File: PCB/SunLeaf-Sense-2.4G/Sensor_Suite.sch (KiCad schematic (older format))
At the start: 0 parts

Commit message: Sensors Added
Sensors added to schematic page, project setup around new 2G module from ST
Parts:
- added M?: SCD30, AVR-KiCAD-Lib-Modules:MODULE_SCD30, symbol AVR-KiCAD-Lib-Modules:SCD30
- added U?: AS7341-DLGT, AVR-KiCAD-Lib-ICs:AS7341-DLGT, symbol AVR-KiCAD-Lib-ICs:AS7341-DLGT
- added U? (x2): HDC1080DMBR, AVR-KiCAD-Lib-ICs:HDC1080DMBR, symbol AVR-KiCAD-Lib-ICs:HDC1080DMBR
- added U?: TPIS1T1086_L5.5, AVR-KiCAD-Lib-ICs:TPIS 1T 1086 L5.5, symbol AVR-KiCAD-Lib-ICs:TPIS1T1086_L5.5
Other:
- note added: "CO2 Sensor Module"
- note added: "Light Spectrum Sensor"
- note added: "Optical IR Sensor"
- note added: "Temperature and Humidity Sensors"
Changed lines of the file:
@@
 $Descr A4 11693 8268
 encoding utf-8
-Sheet 1 5
+Sheet 3 4
 Title ""
 Date ""
@@
 Comment4 ""
 $EndDescr
+$Comp
+L AVR-KiCAD-Lib-Modules:SCD30 M?
+U 1 1 603BC534
+P 3100 3200
+F 0 "M?" H 3150 3250 50  0000 C CNN
+F 1 "SCD30" H 3150 3400 50  0001 C CNN
+F 2 "AVR-KiCAD-Lib-Modules:MODULE_SCD30" H 2900 3200 50  0001 C CNN
+F 3 "https://media.digikey.com/pdf/Data%20Sheets/Sensirion%20PDFs/CD_DS_SCD30_Datasheet_D1.pdf" H 3000 3300 50  0001 C CNN
+F 4 "54.00000" H 3200 3450 50  0001 C CNN "Cost QTY: 1"
+F 5 "*" H 3300 3550 50  0001 C CNN "Cost QTY: 1000"
+F 6 "*" H 3400 3650 50  0001 C CNN "Cost QTY: 2500"
+F 7 "*" H 3500 3750 50  0001 C CNN "Cost QTY: 5000"
+F 8 "*" H 3600 3850 50  0001 C CNN "Cost QTY: 10000"
+F 9 "Sensirion AG" H 3700 3950 50  0001 C CNN "MFR"
+F 10 "SCD30" H 3800 4050 50  0001 C CNN "MFR#"
+F 11 "Digikey" H 3900 4150 50  0001 C CNN "Vendor"
+F 12 "1649-1098-ND" H 4000 4250 50  0001 C CNN "Vendor #"
+F 13 "AVR" H 4100 4350 50  0001 C CNN "Designer"
+F 14 "*" H 4200 4450 50  0001 C CNN "Height"
+F 15 "2/25/2021" H 5300 5550 50  0001 C CNN "Date Created"
+F 16 "2/25/2021" H 4300 4550 50  0001 C CNN "Date Modified"
+F 17 "Yes" H 4400 4650 50  0001 C CNN "Lead-Free ?"
+F 18 "1" H 4500 4750 50  0001 C CNN "RoHS Levels"
+F 19 "ThroughHole" H 4600 4850 50  0001 C CNN "Mounting"
+F 20 "7" H 4700 4950 50  0001 C CNN "Pin Count #"
+F 21 "Active" H 4800 5050 50  0001 C CNN "Status"
+F 22 "*" H 4900 5150 50  0001 C CNN "Tolerance"
+F 23 "CO2 Sensor" H 5000 5250 50  0001 C CNN "Type"
+F 24 "3.3V-5.5V" H 5100 5350 50  0001 C CNN "Voltage"
+F 25 "*" H 5200 5500 50  0001 C CNN "Package"
+F 26 "Carbon Dioxide (CO2) Sensor I²C, Modbus, PWM" H 5500 5800 50  0001 C CNN "Description"
+F 27 "SCD30" H 3200 2350 50  0000 C CNN "_Value_"
+F 28 "*" H 5500 5800 50  0001 C CNN "Management_ID"
+	1    3100 3200
+	1    0    0    -1
+$EndComp
+$Comp
+L AVR-KiCAD-Lib-ICs:AS7341-DLGT U?
+U 1 1 603BEEB8
+P 8900 3050
+F 0 "U?" H 8950 3100 50  0000 C CNN
+F 1 "AS7341-DLGT" H 9000 3250 50  0001 C CNN
+F 2 "AVR-KiCAD-Lib-ICs:AS7341-DLGT" H 8800 2850 50  0001 C CNN
+F 3 "https://media.digikey.com/pdf/Data%20Sheets/Austriamicrosystems%20PDFs/AS7341_DS.pdf" H 8900 2950 50  0001 C CNN
+F 4 "6.75000" H 9000 3300 50  0001 C CNN "Cost QTY: 1"
+F 5 "4.20000" H 9100 3400 50  0001 C CNN "Cost QTY: 1000"
+F 6 "*" H 9200 3500 50  0001 C CNN "Cost QTY: 2500"
+F 7 "*" H 9300 3600 50  0001 C CNN "Cost QTY: 5000"
+F 8 "*" H 9400 3700 50  0001 C CNN "Cost QTY: 10000"
+F 9 "AMS" H 9500 3800 50  0001 C CNN "MFR"
+F 10 "AS7341-DLGT" H 9600 3900 50  0001 C CNN "MFR#"
+F 11 "Digikey" H 9700 4000 50  0001 C CNN "Vendor"
+F 12 "AS7341-DLGTTR-ND" H 9800 4100 50  0001 C CNN "Vendor #"
+F 13 "AVR" H 9900 4200 50  0001 C CNN "Designer"
+F 14 "1mm" H 10000 4300 50  0001 C CNN "Height"
+F 15 "2/25/2021" H 11100 5400 50  0001 C CNN "Date Created"
+F 16 "2/25/2021" H 10100 4400 50  0001 C CNN "Date Modified"
+F 17 "Yes" H 10200 4500 50  0001 C CNN "Lead-Free ?"
+F 18 "1" H 10300 4600 50  0001 C CNN "RoHS Levels"
+F 19 "SMT" H 10400 4700 50  0001 C CNN "Mounting"
+F 20 "8" H 10500 4800 50  0001 C CNN "Pin Count #"
+F 21 "Active" H 10600 4900 50  0001 C CNN "Status"
+F 22 "*" H 10700 5000 50  0001 C CNN "Tolerance"
+F 23 "Light Sensor" H 10800 5100 50  0001 C CNN "Type"
+F 24 "1.8V" H 10900 5200 50  0001 C CNN "Voltage"
+F 25 "8-TFLGA" H 11000 5350 50  0001 C CNN "Package"
+F 26 "Optical Sensor Ambient  I²C 8-TFLGA" H 11300 5650 50  0001 C CNN "Description"
+F 27 "AS7341-DLGT" H 9150 2500 50  0000 C CNN "_Value_"
+F 28 "*" H 11300 5650 50  0001 C CNN "Management_ID"
+	1    8900 3050
+	1    0    0    -1
+$EndComp
+$Comp
+L AVR-KiCAD-Lib-ICs:HDC1080DMBR U?
+U 1 1 603C9047
+P 9450 4350
+F 0 "U?" H 10000 4400 50  0000 C CNN
+F 1 "HDC1080DMBR" H 9500 4450 50  0001 C CNN
+F 2 "AVR-KiCAD-Lib-ICs:HDC1080DMBR" H 9550 4950 50  0001 C CNN
+F 3 "https://www.ti.com/lit/ds/symlink/hdc1080.pdf?HQS=dis-dk-null-digikeymode-dsf-pf-null-wwe&ts=1614238925919" H 9350 4350 50  0001 C CNN
+F 4 "2.80000" H 9550 4600 50  0001 C CNN "Cost QTY: 1"
+F 5 "1.53120" H 9650 4700 50  0001 C CNN "Cost QTY: 1000"
+F 6 "*" H 9750 4800 50  0001 C CNN "Cost QTY: 2500"
+F 7 "*" H 9850 4900 50  0001 C CNN "Cost QTY: 5000"
+F 8 "*" H 9950 5000 50  0001 C CNN "Cost QTY: 10000"
+F 9 "Texas Instruments" H 10050 5100 50  0001 C CNN "MFR"
+F 10 "HDC1080DMBR" H 10150 5200 50  0001 C CNN "MFR#"
+F 11 "Digikey" H 10250 5300 50  0001 C CNN "Vendor"
+F 12 "296-46272-2-ND" H 10350 5400 50  0001 C CNN "Vendor #"
+F 13 "AVR" H 10450 5500 50  0001 C CNN "Designer"
+F 14 "0.8mm" H 10550 5600 50  0001 C CNN "Height"
+F 15 "2/25/2021" H 11650 6700 50  0001 C CNN "Date Created"
+F 16 "2/25/2021" H 10650 5700 50  0001 C CNN "Date Modified"
+F 17 "Yes" H 10750 5800 50  0001 C CNN "Lead-Free ?"
+F 18 "1" H 10850 5900 50  0001 C CNN "RoHS Levels"
+F 19 "SMT" H 10950 6000 50  0001 C CNN "Mounting"
+F 20 "6" H 11050 6100 50  0001 C CNN "Pin Count #"
+F 21 "Active" H 11150 6200 50  0001 C CNN "Status"
+F 22 "*" H 11250 6300 50  0001 C CNN "Tolerance"
+F 23 "Temp/Humid Sensor" H 11350 6400 50  0001 C CNN "Type"
+F 24 "2.7-5.5V" H 11450 6500 50  0001 C CNN "Voltage"
+F 25 "6-WASON" H 11550 6650 50  0001 C CNN "Package"
+F 26 "Humidity Temperature Sensor 0 ~ 100% RH I²C ±2% RH 15s Surface Mount" H 11850 6950 50  0001 C CNN "Description"
+F 27 "HDC1080DMBR" H 9750 3700 50  0000 C CNN "_Value_"
+F 28 "*" H 11850 6950 50  0001 C CNN "Management_ID"
+	1    9450 4350
+	-1   0    0    -1
+$EndComp
+$Comp
+L AVR-KiCAD-Lib-ICs:HDC1080DMBR U?
+U 1 1 603CFAB5
+P 9450 5400
+F 0 "U?" H 10000 5450 50  0000 C CNN
+F 1 "HDC1080DMBR" H 9500 5500 50  0001 C CNN
+F 2 "AVR-KiCAD-Lib-ICs:HDC1080DMBR" H 9550 6000 50  0001 C CNN
+F 3 "https://www.ti.com/lit/ds/symlink/hdc1080.pdf?HQS=dis-dk-null-digikeymode-dsf-pf-null-wwe&ts=1614238925919" H 9350 5400 50  0001 C CNN
+F 4 "2.80000" H 9550 5650 50  0001 C CNN "Cost QTY: 1"
+F 5 "1.53120" H 9650 5750 50  0001 C CNN "Cost QTY: 1000"
+F 6 "*" H 9750 5850 50  0001 C CNN "Cost QTY: 2500"
+F 7 "*" H 9850 5950 50  0001 C CNN "Cost QTY: 5000"
+F 8 "*" H 9950 6050 50  0001 C CNN "Cost QTY: 10000"
+F 9 "Texas Instruments" H 10050 6150 50  0001 C CNN "MFR"
+F 10 "HDC1080DMBR" H 10150 6250 50  0001 C CNN "MFR#"
+F 11 "Digikey" H 10250 6350 50  0001 C CNN "Vendor"
+F 12 "296-46272-2-ND" H 10350 6450 50  0001 C CNN "Vendor #"
+F 13 "AVR" H 10450 6550 50  0001 C CNN "Designer"
+F 14 "0.8mm" H 10550 6650 50  0001 C CNN "Height"
+F 15 "2/25/2021" H 11650 7750 50  0001 C CNN "Date Created"
+F 16 "2/25/2021" H 10650 6750 50  0001 C CNN "Date Modified"
+F 17 "Yes" H 10750 6850 50  0001 C CNN "Lead-Free ?"
+F 18 "1" H 10850 6950 50  0001 C CNN "RoHS Levels"
+F 19 "SMT" H 10950 7050 50  0001 C CNN "Mounting"
+F 20 "6" H 11050 7150 50  0001 C CNN "Pin Count #"
+F 21 "Active" H 11150 7250 50  0001 C CNN "Status"
+F 22 "*" H 11250 7350 50  0001 C CNN "Tolerance"
+F 23 "Temp/Humid Sensor" H 11350 7450 50  0001 C CNN "Type"
+F 24 "2.7-5.5V" H 11450 7550 50  0001 C CNN "Voltage"
+F 25 "6-WASON" H 11550 7700 50  0001 C CNN "Package"
+F 26 "Humidity Temperature Sensor 0 ~ 100% RH I²C ±2% RH 15s Surface Mount" H 11850 8000 50  0001 C CNN "Description"
+F 27 "HDC1080DMBR" H 9750 4750 50  0000 C CNN "_Value_"
+F 28 "*" H 11850 8000 50  0001 C CNN "Management_ID"
+	1    9450 5400
+	-1   0    0    -1
+$EndComp
+Text Notes 8550 4100 0    50   ~ 0
+Temperature and Humidity Sensors
+Text Notes 8700 2850 0    50   ~ 0
+Light Spectrum Sensor
+Text Notes 3050 2900 0    50   ~ 0
+CO2 Sensor Module
+$Comp
+L AVR-KiCAD-Lib-ICs:TPIS1T1086_L5.5 U?
+U 1 1 603E671A
+P 9450 1550
+F 0 "U?" H 10000 1600 50  0000 C CNN
+F 1 "TPIS1T1086_L5.5" H 8700 2150 50  0001 C CNN
+F 2 "AVR-KiCAD-Lib-ICs:TPIS 1T 1086 L5.5" H 8450 1950 50  0001 C CNN
+F 3 "https://media.digikey.com/pdf/Data%20Sheets/Excelitas%20PDFs/TPiS_1T_1086.pdf" H 8550 2050 50  0001 C CNN
+F 4 "15.92000" H 9550 1800 50  0001 C CNN "Cost QTY: 1"
+F 5 "8.93750" H 9650 1900 50  0001 C CNN "Cost QTY: 1000"
+F 6 "*" H 9750 2000 50  0001 C CNN "Cost QTY: 2500"
+F 7 "8.64500" H 9850 2100 50  0001 C CNN "Cost QTY: 5000"
+F 8 "*" H 9950 2200 50  0001 C CNN "Cost QTY: 10000"
+F 9 "Excelitas Technologies" H 10050 2300 50  0001 C CNN "MFR"
+F 10 "TPIS 1T 1086 L5.5" H 10150 2400 50  0001 C CNN "MFR#"
+F 11 "Digikey" H 10250 2500 50  0001 C CNN "Vendor"
+F 12 "1601-1013-ND" H 10350 2600 50  0001 C CNN "Vendor #"
+F 13 "AVR" H 10450 2700 50  0001 C CNN "Designer"
+F 14 "8.35mm" H 10550 2800 50  0001 C CNN "Height"
+F 15 "2/25/2021" H 11650 3900 50  0001 C CNN "Date Created"
+F 16 "2/25/2021" H 10650 2900 50  0001 C CNN "Date Modified"
+F 17 "Yes" H 10750 3000 50  0001 C CNN "Lead-Free ?"
+F 18 "1" H 10850 3100 50  0001 C CNN "RoHS Levels"
+F 19 "ThroughHole" H 10950 3200 50  0001 C CNN "Mounting"
+F 20 "6" H 11050 3300 50  0001 C CNN "Pin Count #"
+F 21 "Active" H 11150 3400 50  0001 C CNN "Status"
+F 22 "*" H 11250 3500 50  0001 C CNN "Tolerance"
+F 23 "*" H 11350 3600 50  0001 C CNN "Type"
+F 24 "2.6-3.6V" H 11450 3700 50  0001 C CNN "Voltage"
+F 25 "Radial Can" H 11550 3850 50  0001 C CNN "Package"
+F 26 "Optical Sensor IR  I²C Radial, Metal Can" H 11850 4150 50  0001 C CNN "Description"
+F 27 "TPIS 1T 1086 L5.5" H 9750 800 50  0000 C CNN "_Value_"
+F 28 "*" H 11850 4150 50  0001 C CNN "Management_ID"
+	1    9450 1550
+	-1   0    0    -1
+$EndComp
+Text Notes 8800 1400 0    50   ~ 0
+Optical IR Sensor
 $EndSCHEMATC

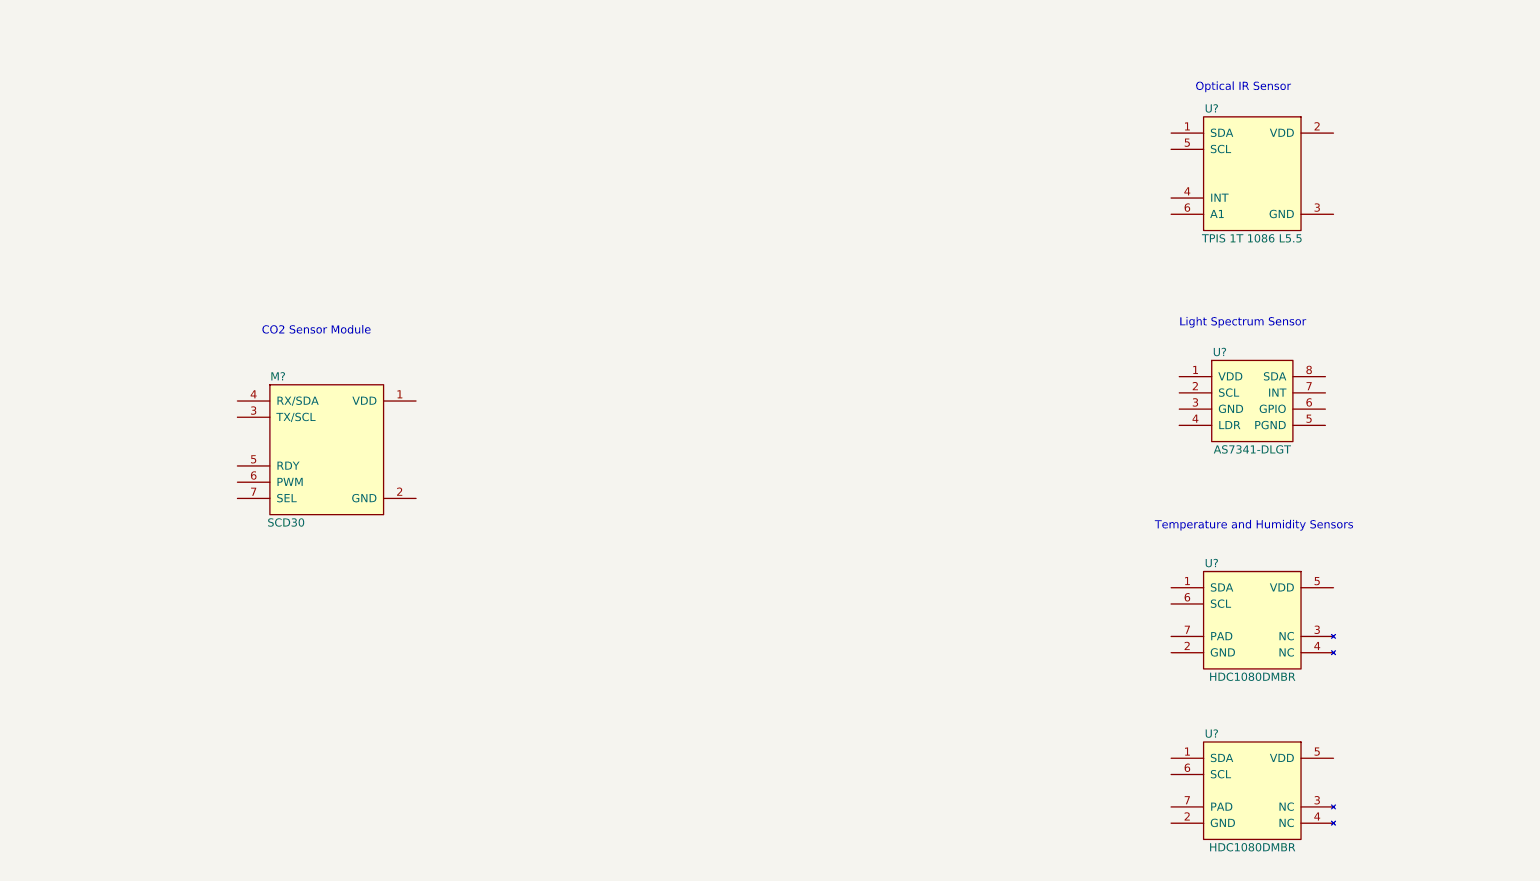
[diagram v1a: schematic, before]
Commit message: PCB
PCB started, PAR sensor circuitry integrated into design
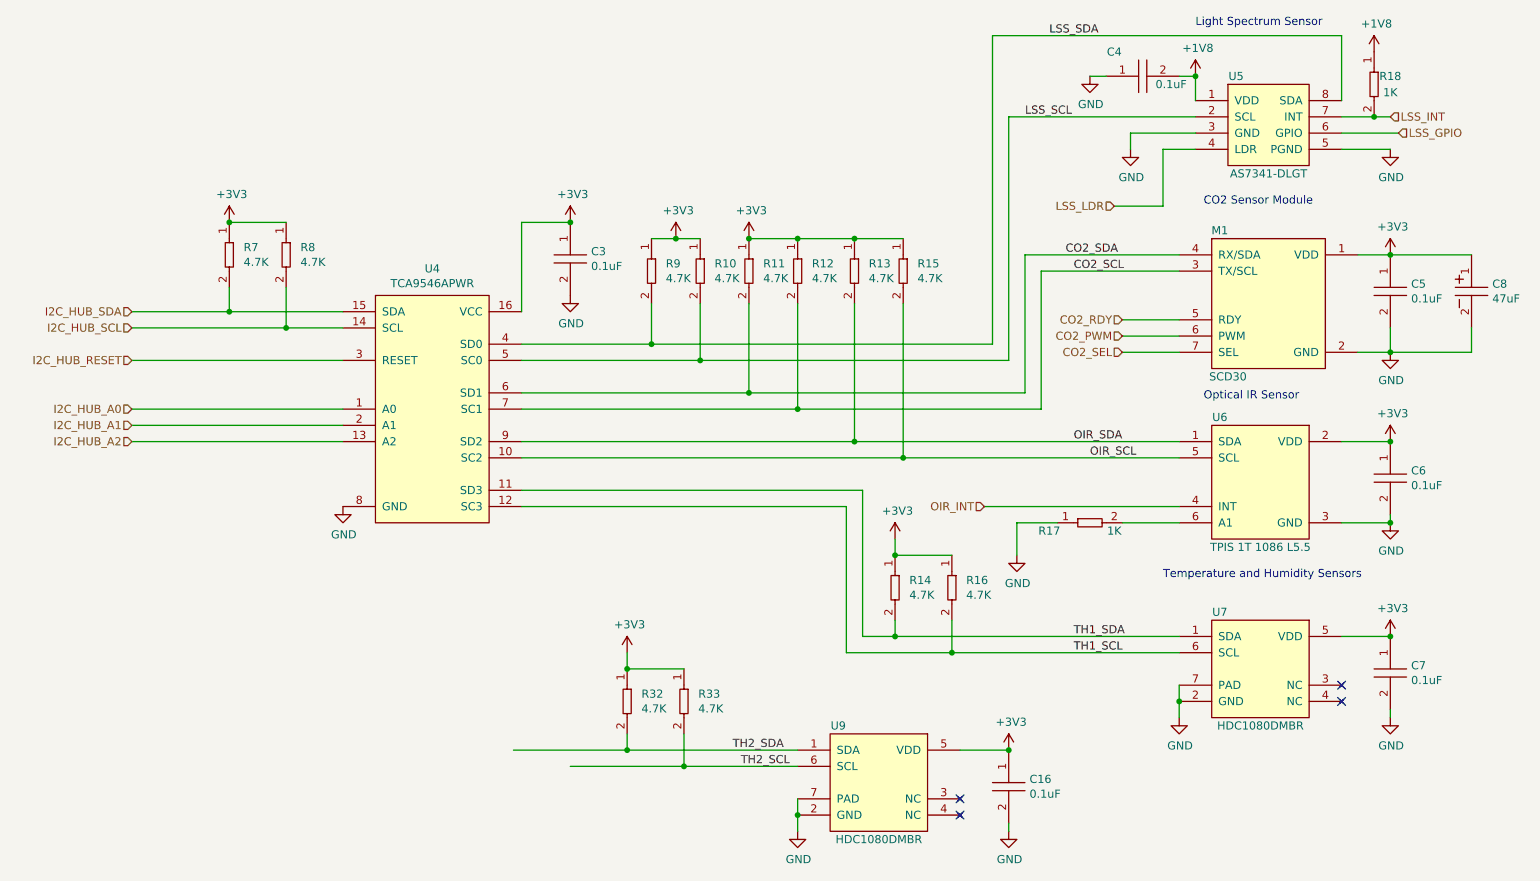
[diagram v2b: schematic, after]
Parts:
- removed U?: HDC1080DMBR, AVR-KiCAD-Lib-ICs:HDC1080DMBR, symbol AVR-KiCAD-Lib-ICs:HDC1080DMBR
- added C16, C3, C4, C5, C6, C7: C0402C104K9PACTU, AVR-KiCAD-Lib-Resistors:R0402, symbol AVR-KiCAD-Lib-Capacitors:C0402C104K9PACTU
- added C8: UCM1C470MCL1GS, AVR-KiCAD-Lib-Capacitors:UCM1C470MCL1GS, symbol AVR-KiCAD-Lib-Capacitors:UCM1C470MCL1GS
- added R10, R11, R12, R13, R14, R15, R16, R32, R33, R7, R8, R9: RC0402FR-074K7L, AVR-KiCAD-Lib-Resistors:R0402, symbol AVR-KiCAD-Lib-Resistors:RC0402FR-074K7L
- added R17, R18: RC0402FR-071KL, AVR-KiCAD-Lib-Resistors:R0402, symbol AVR-KiCAD-Lib-Resistors:RC0402FR-071KL
- added U4: TCA9546APWR, growbox-KiCAD-ICs:PW0016A, symbol AVR-KiCAD-Lib-ICs:TCA9546APWR
- added U9: HDC1080DMBR, AVR-KiCAD-Lib-ICs:HDC1080DMBR, symbol AVR-KiCAD-Lib-ICs:HDC1080DMBR
- U6: renamed from U?; footprint AVR-KiCAD-Lib-ICs:TPIS 1T 1086 L5.5 -> AVR-KiCAD-Lib-ICs:TPIS1T1086L5.5
- gave numbers to parts that had none: 3
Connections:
- net +3V3: now reaches M1.1 (VDD)
- net +3V3: now also U6.2 (VDD), U7.5 (VDD), C16.1, C3.1, C5.1, C6.1, C7.1, C8.1, R10.1, R11.1, R12.1, R13.1, R14.1, R15.1, R16.1, R32.1, R33.1, R7.1, R8.1, R9.1, U4.16 (VCC), U9.5 (VDD)
- net GND: now reaches M1.2 (GND)
- net GND: now also U5.3 (GND), U5.5 (PGND), U6.3 (GND), U7.2 (GND), U7.7 (PAD), C16.2, C3.2, C4.1, C5.2, C6.2, C7.2, C8.2, R17.1, U4.8 (GND), U9.2 (GND), U9.7 (PAD)
- net CO2_SCL: now reaches M1.3 (TX/SCL)
- net CO2_SCL: now also R12.2, U4.7 (SC1)
- net CO2_SDA: now reaches M1.4 (RX/SDA)
- net CO2_SDA: now also R11.2, U4.6 (SD1)
- net CO2_RDY: now reaches M1.5 (RDY)
- net CO2_PWM: now reaches M1.6 (PWM)
- net CO2_SEL: now reaches M1.7 (SEL)
- net +1V8: now reaches U5.1 (VDD)
- net +1V8: now also C4.2, R18.1
- net LSS_SCL: now reaches U5.2 (SCL)
- net LSS_SCL: now also R10.2, U4.5 (SC0)
- net LSS_LDR: now reaches U5.4 (LDR)
- net LSS_GPIO: now reaches U5.6 (GPIO)
- net LSS_INT: now reaches U5.7 (INT)
- net LSS_INT: now also R18.2
- net LSS_SDA: now reaches U5.8 (SDA)
- net LSS_SDA: now also R9.2, U4.4 (SD0)
- net TH1_SDA: now reaches U7.1 (SDA)
- net TH1_SDA: now also R14.2, U4.11 (SD3)
- net TH1_SCL: now reaches U7.6 (SCL)
- net TH1_SCL: now also R16.2, U4.12 (SC3)
- net OIR_SDA: now reaches U6.1 (SDA)
- net OIR_SDA: now also R13.2, U4.9 (SD2)
- net OIR_INT: now reaches U6.4 (INT)
- net OIR_SCL: now reaches U6.5 (SCL)
- net OIR_SCL: now also R15.2, U4.10 (SC2)
- net at U6.6 (A1): now also R17.2
- new net I2C_HUB_A0: U4.1 (A0)
- new net I2C_HUB_A1: U4.2 (A1)
- new net I2C_HUB_A2: U4.13 (A2)
- new net I2C_HUB_RESET: U4.3 (RESET)
- new net I2C_HUB_SCL: R8.2, U4.14 (SCL)
- new net I2C_HUB_SDA: R7.2, U4.15 (SDA)
- new net TH2_SCL: R33.2, U9.6 (SCL)
- new net TH2_SDA: R32.2, U9.1 (SDA)
- no-connect marks 0 -> 4
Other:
- moved on the sheet: M1, U5, U6, U7
